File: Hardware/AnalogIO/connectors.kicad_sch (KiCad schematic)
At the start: 6 parts, among them J1 ANALOG INPUTS, J2 ANALOG OUTPUTS, J3 Conn_02x23_Odd_Even, J4 Conn_02x23_Odd_Even

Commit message: schematic update & pcb update
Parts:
- renumbered D5 to D3, D3 to D4
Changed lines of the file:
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@@
 		(dnp no)
 		(fields_autoplaced yes)
-		(property "Reference" "D5"
+		(property "Reference" "D3"
 			(at 68.58 78.7399 90)
 			(effects
@@
 			(project ""
 				(path "/b652b05a-4e3d-4ad1-b032-18886abe7d45/d5b0e62d-bd3f-4f7d-ae0f-b864e773d760"
-					(reference "D5")
+					(reference "D3")
 					(unit 1)
 				)
@@
 		(dnp no)
 		(fields_autoplaced yes)
-		(property "Reference" "D3"
+		(property "Reference" "D4"
 			(at 83.82 78.7399 90)
 			(effects
@@
 			(project "analogIO"
 				(path "/b652b05a-4e3d-4ad1-b032-18886abe7d45/d5b0e62d-bd3f-4f7d-ae0f-b864e773d760"
-					(reference "D3")
+					(reference "D4")
 					(unit 1)
 				)

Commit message: schematic update & pcb update
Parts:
- J3: value Conn_02x23_Odd_Even -> NUCLEO LEFT; footprint PLC_STM_Power:PRT12790 -> PLC_STM:PRT12790
- J4: value Conn_02x23_Odd_Even -> NUCLEO RIGHT; footprint PLC_STM_Power:PRT12790 -> PLC_STM:PRT12790
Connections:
- net VIN is gone; now on net +5V: J3.15 (Pin_15)
- net +15V: now reaches J4.21 (Pin_21)
- net -15V: now reaches J3.18 (Pin_18)
- net 3V3 renamed +3V3
- net 5V renamed +5V
- net AI0 renamed AO_0
- net ANALOG_IN10: no longer names the net of J3.21 (Pin_21)
- net ANALOG_IN13: no longer names the net of J3.23 (Pin_23)
- net ANALOG_IN3: no longer names the net of J3.19 (Pin_19)
- net ANALOG_IN3/15: no longer names the net of J3.27 (Pin_27)
- net ANALOG_IN3/5: no longer names the net of J3.42 (Pin_42)
- net ANALOG_IN3/6: no longer names the net of J3.40 (Pin_40)
- net ANALOG_IN3/7: no longer names the net of J3.44 (Pin_44)
- net ANALOG_IN3/8: no longer names the net of J3.29 (Pin_29)
- net ANALOG_IN3/9: no longer names the net of J3.25 (Pin_25)
- net ANALOG_IN6 renamed AI_0
- net ANALOG_IN7 renamed AI_1
- net AO1 renamed AO_1
- no-connect marks 51 -> 54

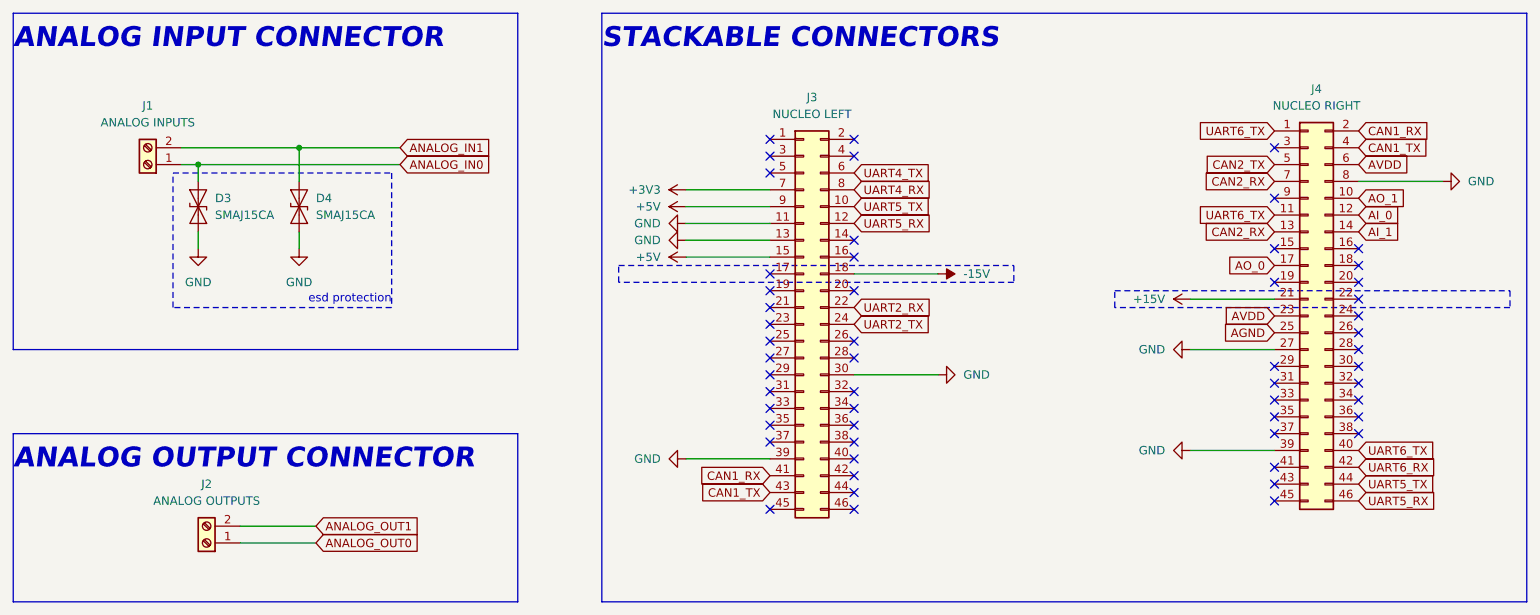
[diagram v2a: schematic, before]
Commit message: analog & can finished
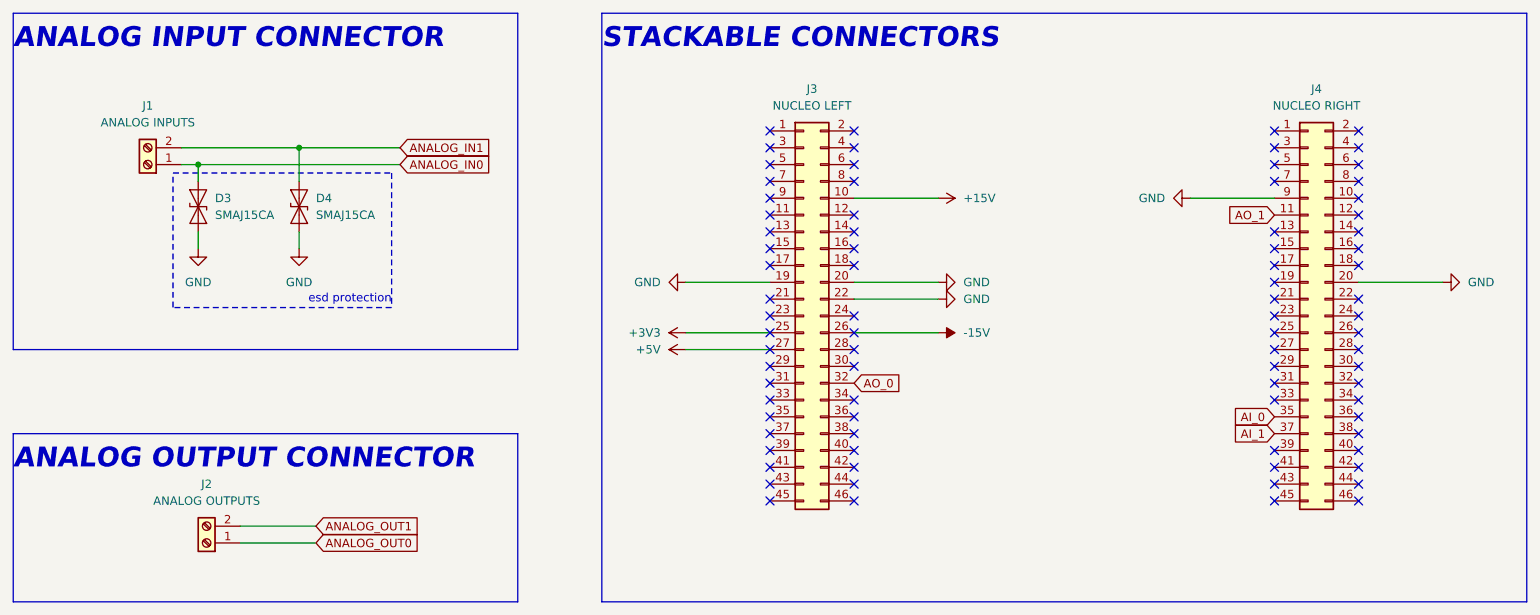
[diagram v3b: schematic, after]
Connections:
- net UART2_RX is gone; now on net GND: J3.22 (Pin_22)
- net +15V: now also J3.10 (Pin_10); no longer J4.21 (Pin_21)
- net +3V3: now also J3.25 (Pin_25); no longer J3.7 (Pin_7)
- net +5V: now also J3.27 (Pin_27); no longer J3.15 (Pin_15), J3.9 (Pin_9)
- net -15V: now also J3.26 (Pin_26); no longer J3.18 (Pin_18)
- net AI_0: now also J4.35 (Pin_35); no longer J4.12 (Pin_12)
- net AI_1: now also J4.37 (Pin_37); no longer J4.14 (Pin_14)
- net AO_0: now also J3.32 (Pin_32); no longer J4.17 (Pin_17)
- net AO_1: now also J4.11 (Pin_11); no longer J4.10 (Pin_10)
- net GND: now also J3.19 (Pin_19), J3.20 (Pin_20), J4.20 (Pin_20), J4.9 (Pin_9); no longer J3.11 (Pin_11), J3.13 (Pin_13), J3.30 (Pin_30), J3.39 (Pin_39), J4.27 (Pin_27), J4.39 (Pin_39), J4.8 (Pin_8)
- net AGND: no longer names the net of J4.25 (Pin_25)
- net AVDD: no longer names the net of J4.23 (Pin_23)
- net AVDD: no longer J4.6 (Pin_6)
- net CAN1_RX: no longer names the net of J4.2 (Pin_2)
- net CAN1_RX: no longer J3.41 (Pin_41)
- net CAN1_TX: no longer names the net of J4.4 (Pin_4)
- net CAN1_TX: no longer J3.43 (Pin_43)
- net CAN2_RX: no longer names the net of J4.13 (Pin_13)
- net CAN2_RX: no longer J4.7 (Pin_7)
- net CAN2_TX: no longer names the net of J4.5 (Pin_5)
- net UART2_TX: no longer names the net of J3.24 (Pin_24)
- net UART4_RX: no longer names the net of J3.8 (Pin_8)
- net UART4_TX: no longer names the net of J3.6 (Pin_6)
- net UART5_RX: no longer names the net of J4.46 (Pin_46)
- net UART5_RX: no longer J3.12 (Pin_12)
- net UART5_TX: no longer names the net of J4.44 (Pin_44)
- net UART5_TX: no longer J3.10 (Pin_10)
- net UART6_RX: no longer names the net of J4.42 (Pin_42)
- removed net UART6_TX: J4.1 (Pin_1), J4.11 (Pin_11), J4.40 (Pin_40)
- no-connect marks 54 -> 82
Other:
- moved on the sheet: J3

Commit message: small adjustments and final revision
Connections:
- no-connect marks 82 -> 79
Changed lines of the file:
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@@
-	)
-	(no_connect
-		(at 165.1 99.06)
 	)
 	(no_connect
@@
 	)
 	(no_connect
-		(at 152.4 101.6)
-	)
-	(no_connect
-		(at 152.4 99.06)
-	)
-	(no_connect
 		(at 241.3 124.46)
 	)
@@
 	(wire
 		(pts
+			(xy 72.39 128.27) (xy 83.82 128.27)
+		)
+		(stroke
+			(width 0)
+			(type default)
+		)
+	)
+	(wire
+		(pts
+			(xy 66.04 73.66) (xy 66.04 76.2)
+		)
+		(stroke
+			(width 0)
+			(type default)
+		)
+	)
+	(wire
+		(pts
 			(xy 165.1 99.06) (xy 177.8 99.06)
 		)
 		(stroke
-			(width 0)
-			(type default)
-		)
-	)
-	(wire
-		(pts
-			(xy 72.39 128.27) (xy 83.82 128.27)
-		)
-		(stroke
-			(width 0)
-			(type default)
-		)
-	)
-	(wire
-		(pts
-			(xy 66.04 73.66) (xy 66.04 76.2)
-		)
-		(stroke
